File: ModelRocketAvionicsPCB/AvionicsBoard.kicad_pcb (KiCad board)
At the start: 2 copper layers, 62 parts, among them CON1 microSD_Card, P1 FTSH-105-01-F-DV, P2 USB_OTG, P3 JST-2, SW1 SW_RST, U1 TM4C123GH6PM, U2 AT25SF161-16Mb_SPI_FLASH, U3 LIS331, U4 L3GD20HTR, U5 MPL3115A2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

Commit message: Began Preliminary Layout
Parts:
- added JP1: Jumper_NO_Small, Avionics:NO_Jumper, F.Cu at (83.7, 126.4)
- added JP2: Jumper_NC_Small, Avionics:NC_Jumper, F.Cu at (86.3, 124.4)
- added JP3: Jumper_NO_Small, Avionics:NO_Jumper, F.Cu at (78.6, 125.2)
- added JP4: Jumper_NC_Small, Avionics:NC_Jumper, F.Cu at (80.5, 124.6)
- moved SW1 114.6 mm to (72.9, 83.3)
- moved C25 103.1 mm to (72.7, 131.3), turned to 90 degrees
- moved Y2 101.8 mm to (89.3, 85.2)
- moved C13 100.1 mm to (76.7, 92.0), turned to 90 degrees
- moved D1 94.7 mm to (95.2, 53.5)
- moved C11 94.0 mm to (75.1, 92.0), turned to 90 degrees
- moved C32 90.5 mm to (106.6, 56.8), turned to 180 degrees
- moved U4 88.9 mm to (75.5, 125.2), turned to 180 degrees
- moved P2 86.8 mm to (71.3, 94.1), turned to 270 degrees
- moved C16 83.5 mm to (88.8, 77.0)
- moved U7 82.1 mm to (105.8, 54.5), turned to 90 degrees
- moved U1 81.5 mm to (99.8, 99.2), turned to 135 degrees
- moved R7 80.4 mm to (66.9, 85.6), turned to 270 degrees
- moved U3 79.7 mm to (83.3, 123.6)
- moved R3 78.7 mm to (73.0, 113.5), turned to 270 degrees
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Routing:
- added copper zone on B.Cu, net PWR_GND
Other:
- net class Default: clearance 0.2 -> 0.15
- rule trace_clearance: 0.2 -> 0.15
- rule trace_min: 0.2 -> 0.15

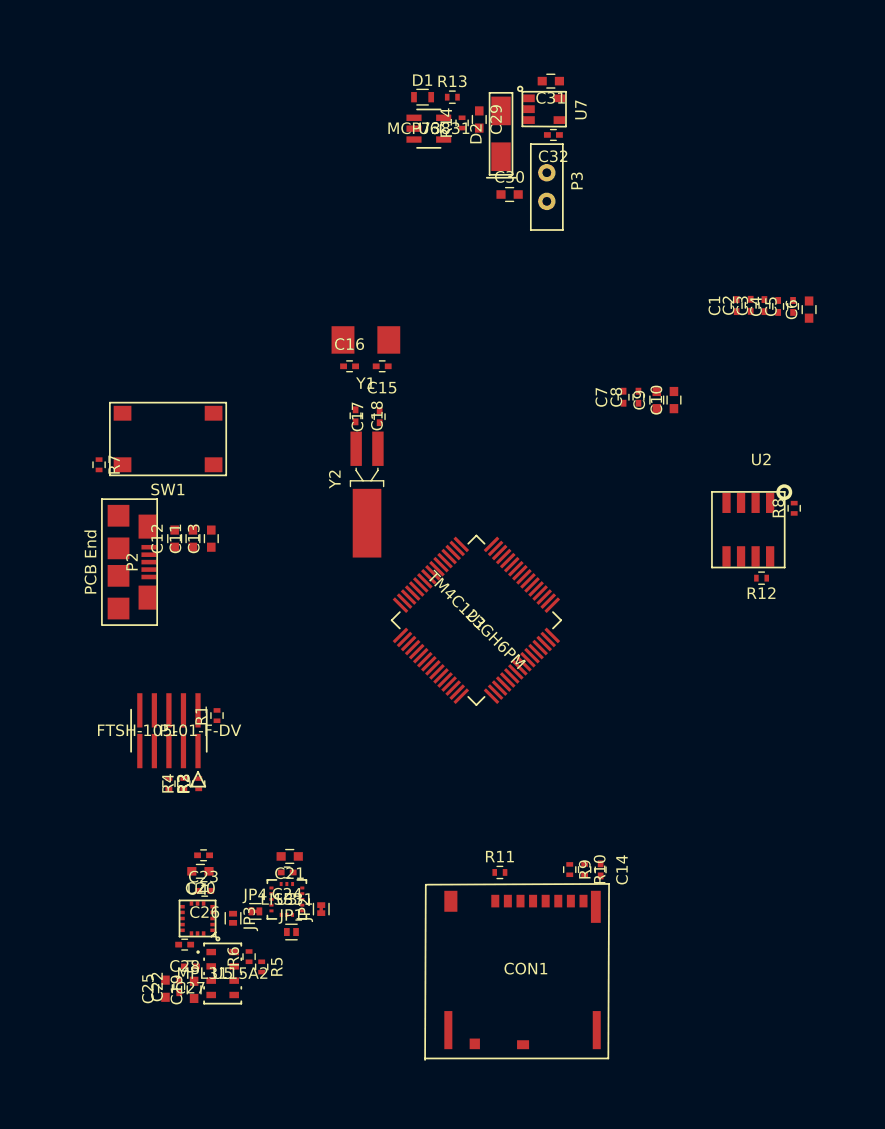
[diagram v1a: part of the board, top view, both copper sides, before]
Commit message: Completed Preliminary Layout
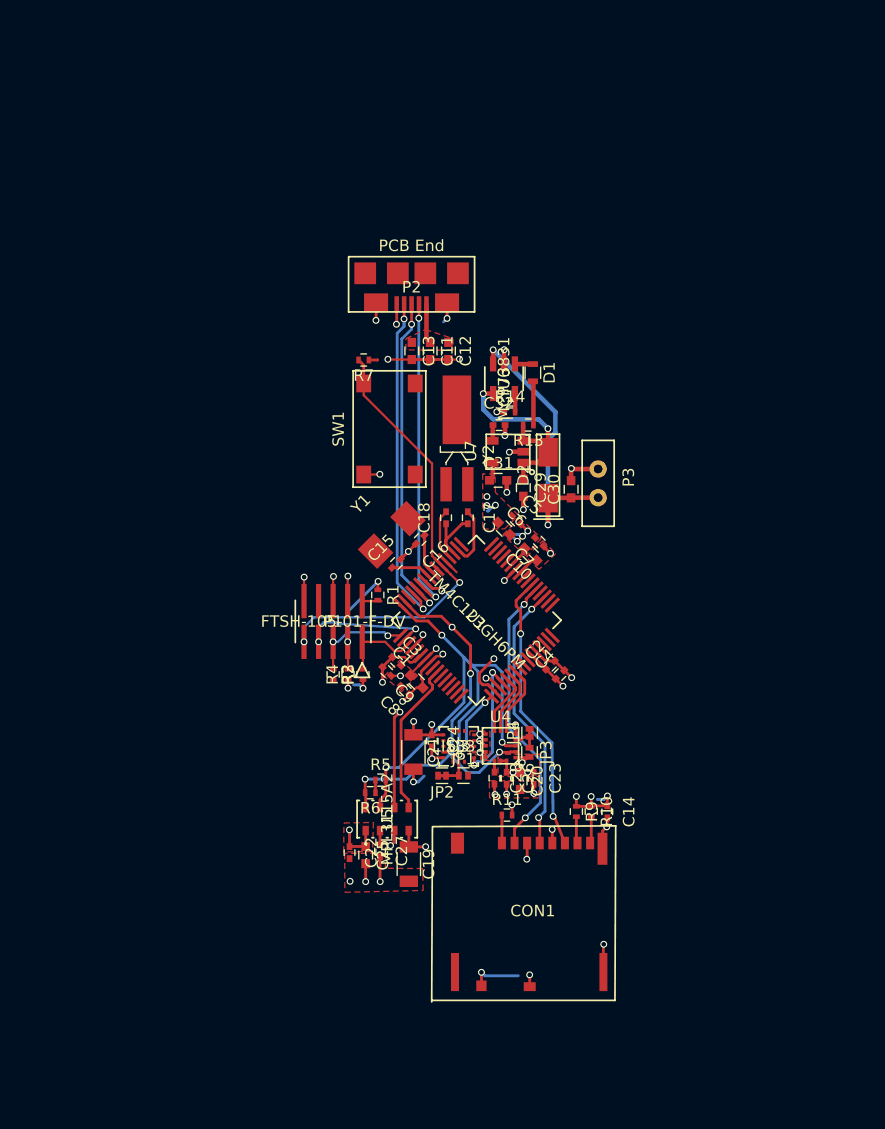
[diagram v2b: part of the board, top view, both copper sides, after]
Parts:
- removed R12, R8: 10k, SFUSAT-Res:R_0402
- removed U2: AT25SF161-16Mb_SPI_FLASH, Avionics:Flash_Mem_AT25SF161-SSHD
- C19, C21: footprint SFUSAT Caps:C_0603 -> SFUSAT Caps:C_1206
- moved C3 44.7 mm to (92.9, 102.8), turned to 315 degrees
- moved C1 44.2 mm to (92.0, 103.7), turned to 315 degrees
- moved C4 37.4 mm to (107.1, 103.9), turned to 45 degrees
- moved C2 36.0 mm to (106.3, 103.1), turned to 45 degrees
- moved C31 35.2 mm to (101.8, 87.0), turned to 0 degrees
- moved C6 32.8 mm to (102.3, 91.2), turned to 315 degrees
- moved C8 32.7 mm to (93.6, 105.3), turned to 135 degrees
- moved C29 32.4 mm to (104.0, 87.6)
- moved C9 32.3 mm to (94.6, 104.5), turned to 135 degrees
- moved P2 32.1 mm to (94.2, 71.6), turned to 180 degrees
- moved C28 30.7 mm to (101.4, 113.0), turned to 270 degrees
- moved C5 30.5 mm to (103.3, 90.4), turned to 315 degrees
- moved U4 30.5 mm to (102.0, 110.1)
- moved D2 30.1 mm to (106.1, 86.5)
- moved U7 30.1 mm to (102.6, 84.5), turned to 270 degrees
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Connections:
- U1 pad 1: Net-(U1-Pad1) -> PB6/ACC_INT1
- U1 pad 4: Net-(U1-Pad4) -> PB7/ACC_INT2
- U1 pad 5: Net-(U1-Pad5) -> PE2/GYR_DEN
- U1 pad 57: Net-(U1-Pad57) -> PB5/BAR_INT1
- U1 pad 58: Net-(U1-Pad58) -> PB4/BAR_INT2
- U1 pad 6: Net-(U1-Pad6) -> PF4/GYR_INT1
- U1 pad 7: Net-(U1-Pad7) -> PE3/GYR_INT2/DRDY
- U3 pad 11: /Sensors/ACC_INT1 -> PB6/ACC_INT1
- U3 pad 9: /Sensors/ACC_INT2 -> PB7/ACC_INT2
- U4 pad 6: /Sensors/GYR_INT2/DRDY -> PE3/GYR_INT2/DRDY
- U4 pad 7: /Sensors/GYR_INT1 -> PF4/GYR_INT1
- U4 pad 8: /Sensors/GYR_DEN -> PE2/GYR_DEN
- U5 pad 5: /Sensors/BAR_INT2 -> PB4/BAR_INT2
- U5 pad 6: /Sensors/BAR_INT1 -> PB5/BAR_INT1
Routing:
- net PWR_GND: track 0.00 -> 74.8 mm, vias 0 -> 41
- net ACC_CS: track 0.00 -> 56.2 mm, vias 0 -> 20
- net PB3/I2C_SDA: track 0.00 -> 45.6 mm, vias 0 -> 4
- net RESET: track 0.00 -> 39.6 mm, vias 0 -> 2
- net PB2/I2C_SCL: track 0.00 -> 36.8 mm, vias 0 -> 5
- net PB0/USB0_ID: track 0.00 -> 29.6 mm, vias 0 -> 2
- net PD5/USB0_DP: track 0.00 -> 29.2 mm, vias 0 -> 2
- net PD4/USB0_DM: track 0.00 -> 28.0 mm, vias 0 -> 2
- net /Power/+VBAT: track 0.00 -> 25.8 mm, vias 0 -> 2
- net PA4/SDDO: track 0.00 -> 25.3 mm, vias 0 -> 2
- net PA5/SDDI: track 0.00 -> 24.7 mm, vias 0 -> 2
- net PA2/SDCLK: track 0.00 -> 24.0 mm, vias 0 -> 2
- net +USB_VBUS: track 0.00 -> 22.4 mm, vias 0 -> 2
- net PB4/BAR_INT2: track 0.00 -> 13.6 mm
- net PC2/JTAG_TDI: track 0.00 -> 11.3 mm, vias 0 -> 2
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- added copper zone on F.Cu, net +USB_VBUS
- added copper zone on F.Cu, net ACC_CS
- added copper zone on PWR.Cu, net ACC_CS
- added copper zone on F.Cu, net PWR_GND
- added copper zone on GND, net PWR_GND
- added copper zone on F.Cu, net PWR_VDDC
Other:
- copper layers 2 -> 4

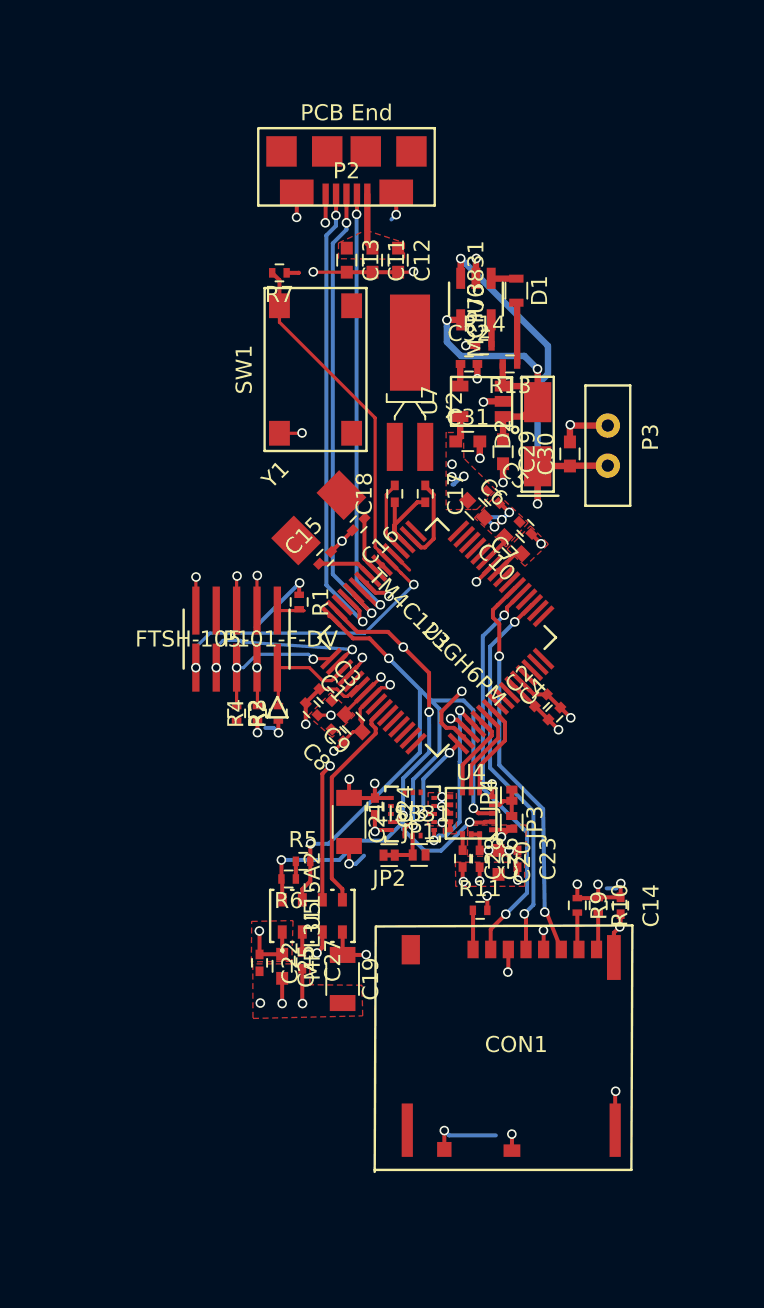
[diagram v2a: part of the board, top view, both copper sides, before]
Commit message: Partially Complete Updated Avionics Layout
Final Pinout and Silk Screen still needs to be completed.
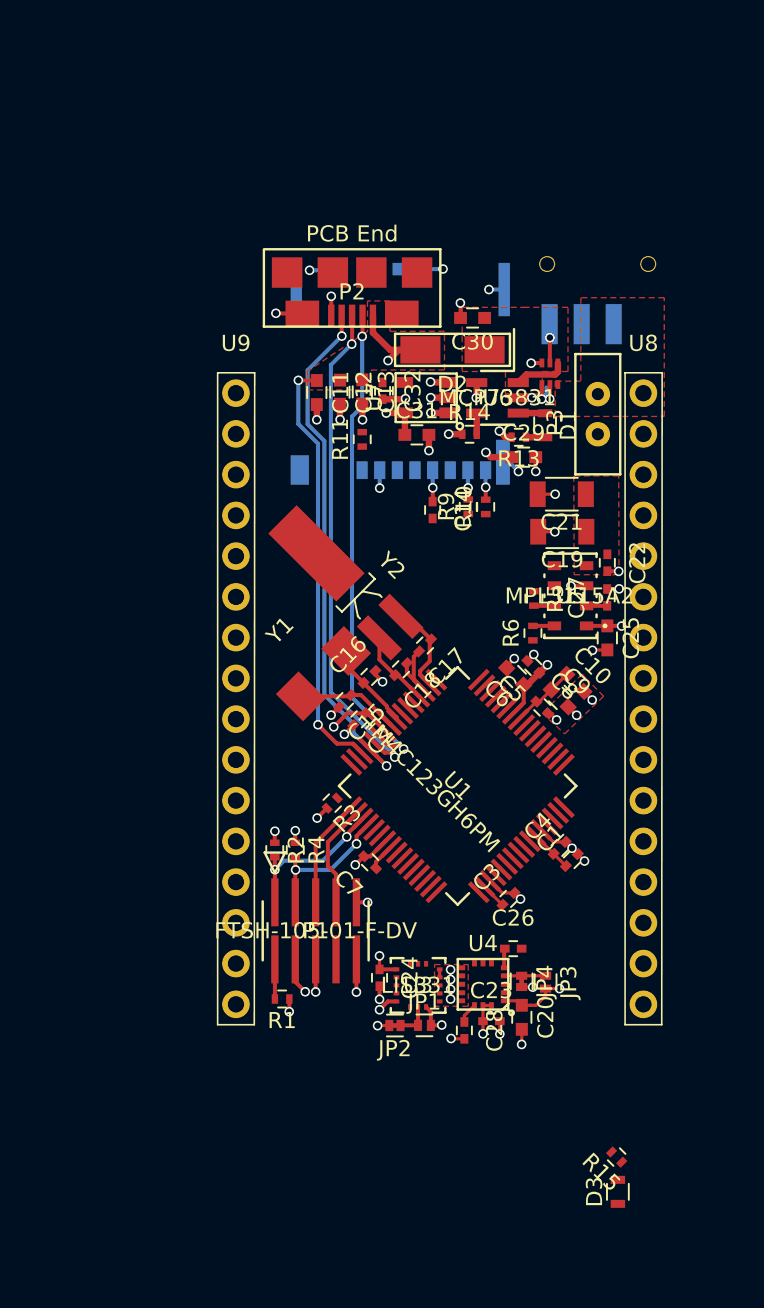
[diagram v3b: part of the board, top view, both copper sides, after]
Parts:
- removed R7: 10k, SFUSAT-Res:R_0402
- removed SW1: SW_RST, Avionics:Push_Button_B3S-1000
- added D3: Led_Small, SFUSAT-Res:R_0603, F.Cu at (111.1, 133.7)
- added R15: 330, SFUSAT-Res:R_0402, F.Cu at (111.0, 131.6)
- added U10: DMG1029SV-7, AvionicsIC:SOT563, F.Cu at (106.9, 82.7)
- added U11: CSS-1210TB, Avionics:CSS-1210TB, B.Cu at (109.8, 77.2)
- added U8: CONNHeaderFemale16, Avionics:16x1_Female_Header, F.Cu at (112.7, 103.0)
- added U9: CONNHeaderFemale16, Avionics:16x1_Female_Header, F.Cu at (87.3, 103.0)
- CON1: moved to B.Cu
- moved CON1 52.9 mm to (91.1, 77.5)
- moved C22 33.0 mm to (110.5, 94.5)
- moved C19 31.1 mm to (107.6, 92.6), turned to 180 degrees
- moved R11 30.3 mm to (95.2, 86.8), turned to 90 degrees
- moved C27 29.6 mm to (110.4, 96.7), turned to 90 degrees
- moved C25 28.8 mm to (110.5, 99.2)
- moved C14 27.3 mm to (99.6, 91.2)
- moved R10 25.8 mm to (102.9, 91.0), turned to 90 degrees
- moved R9 25.8 mm to (101.8, 91.0), turned to 90 degrees
- moved U5 25.6 mm to (108.2, 96.6), turned to 180 degrees
- moved R1 24.8 mm to (90.2, 121.7), turned to 180 degrees
- moved C21 24.4 mm to (107.6, 90.2), turned to 180 degrees
- moved C7 23.0 mm to (95.7, 113.2)
- moved R5 21.8 mm to (105.9, 96.7), turned to 270 degrees
- moved R6 21.6 mm to (105.8, 98.9), turned to 90 degrees
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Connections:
- C30 pad 1: /Power/+VBAT -> +VBAT_ON
- D2 pad 2: /Power/+VBAT -> +VBAT_ON
- P3 pad 1: /Power/+VBAT -> +VBAT
- R3 pad 2: Net-(R3-Pad2) -> PWR_GND
- U1 pad 52: PC1/JTAG_TCK -> PC0/JTAG_TCK
- U1 pad 8: Net-(U1-Pad8) -> PE1/IND_LED
- U6 pad 3: /Power/+VBAT -> +VBAT_ON
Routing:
- net PB3/I2C_SDA: track 45.6 -> 1.28 mm, vias 4 -> 0
- net RESET: track 39.6 -> 0.70 mm, vias 2 -> 1
- net PB2/I2C_SCL: track 36.8 -> 1.34 mm, vias 5 -> 0
- net /Power/+VBAT: track 25.8 -> 0.00 mm, vias 2 -> 0
- net PA5/SDDI: track 24.7 -> 0.00 mm, vias 2 -> 0
- net PA4/SDDO: track 25.3 -> 1.12 mm, vias 2 -> 1
- net PA2/SDCLK: track 24.0 -> 0.00 mm, vias 2 -> 0
- net ACC_CS: track 56.2 -> 33.0 mm, vias 20 -> 12
- net PWR_GND: track 74.8 -> 56.0 mm, vias 41 -> 48
- net +USB_VBUS: track 22.4 -> 39.2 mm, vias 2 -> 8
- net PB4/BAR_INT2: track 13.6 -> 0.00 mm
- net PB7/ACC_INT2: track 11.1 -> 0.00 mm, vias 2 -> 0
- net PB5/BAR_INT1: track 8.55 -> 0.00 mm, vias 1 -> 0
- net PC0/JTAG_TCK: track 2.41 -> 8.83 mm, vias 1 -> 2
- net PE3/GYR_INT2/DRDY: track 6.11 -> 0.00 mm
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- added copper zone on PWR.Cu, net +USB_VBUS
- added copper zone on F.Cu, net +VBAT
- added copper zone on F.Cu, net +VBAT_ON
- removed copper zone on F.Cu, net PWR_VDDC

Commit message: CDR Ready Board
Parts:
- Off U11 On: renamed from U11
- U10: value DMG1029SV-7 -> PMOS
- moved C24 8.21 mm to (99.5, 127.9), turned to 0 degrees
- moved R15 7.87 mm to (109.9, 123.8), turned to 90 degrees
- moved D3 7.52 mm to (109.9, 126.3)
- moved JP3 7.27 mm to (100.0, 117.6), turned to 0 degrees
- moved C26 6.68 mm to (98.0, 119.6), turned to 90 degrees
- moved JP2 6.38 mm to (102.5, 127.0), turned to 270 degrees
- moved JP4 5.60 mm to (99.7, 119.1), turned to 0 degrees
- moved U8 5.00 mm to (112.7, 108.0), turned to 180 degrees
- moved U9 5.00 mm to (87.3, 108.0), turned to 180 degrees
- moved U3 4.84 mm to (100.0, 125.5), turned to 90 degrees
- moved C20 4.59 mm to (102.6, 119.0), turned to 0 degrees
- moved R11 4.33 mm to (95.5, 91.2), turned to 270 degrees
- moved JP1 3.85 mm to (102.5, 125.1), turned to 90 degrees
- moved U4 2.87 mm to (99.9, 121.5), turned to 270 degrees
- moved C23 2.37 mm to (102.2, 121.0), turned to 90 degrees
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- renumbered CON1 to microSD_Card
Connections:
- net Net-(U1-Pad28) renamed PF0
- net Net-(U1-Pad29) renamed PF1
- net PD4/USB0_DM renamed USB0_D-
- net PD5/USB0_DP renamed USB0_D+
- net PE2/GYR_DEN renamed PF4/GYR_DEN
- U1 pad 1: PB6/ACC_INT1 -> PB6/GYR_INT2/DRDY
- U1 pad 10: Net-(U1-Pad10) -> PD7
- U1 pad 13: Net-(U1-Pad13) -> PC7
- U1 pad 14: Net-(U1-Pad14) -> PC6
- U1 pad 15: Net-(U1-Pad15) -> PC5
- U1 pad 16: Net-(U1-Pad16) -> PC4
- U1 pad 17: Net-(U1-Pad17) -> PA0/U0Rx
- U1 pad 18: Net-(U1-Pad18) -> PA1/U0Tx
- U1 pad 23: Net-(U1-Pad23) -> PA6
- U1 pad 24: Net-(U1-Pad24) -> PA7
- U1 pad 30: Net-(U1-Pad30) -> PF2/BAR_INT1
- U1 pad 31: Net-(U1-Pad31) -> PF3/BAR_INT2
- U1 pad 33: Net-(U1-Pad33) -> HIB
- U1 pad 4: PB7/ACC_INT2 -> PB7/GYR_INT1
- U1 pad 53: Net-(U1-Pad53) -> PD6
- U1 pad 57: PB5/BAR_INT1 -> PB5
- U1 pad 58: PB4/BAR_INT2 -> PB4
- U1 pad 59: Net-(U1-Pad59) -> PE4
- U1 pad 6: PF4/GYR_INT1 -> PE3/ACC_INT1
- U1 pad 60: Net-(U1-Pad60) -> PE5
- U1 pad 7: PE3/GYR_INT2/DRDY -> PE2/ACC_INT2
- U1 pad 9: Net-(U1-Pad9) -> PE0
- U3 pad 11: PB6/ACC_INT1 -> PE3/ACC_INT1
- U3 pad 9: PB7/ACC_INT2 -> PE2/ACC_INT2
- U4 pad 6: PE3/GYR_INT2/DRDY -> PB6/GYR_INT2/DRDY
- U4 pad 7: PF4/GYR_INT1 -> PB7/GYR_INT1
- U5 pad 5: PB4/BAR_INT2 -> PF3/BAR_INT2
- U5 pad 6: PB5/BAR_INT1 -> PF2/BAR_INT1
- U8 pad 1: Net-(U8-Pad1) -> +VBAT
- U8 pad 10: Net-(U8-Pad10) -> PC4
- U8 pad 11: Net-(U8-Pad11) -> PC5
- U8 pad 12: Net-(U8-Pad12) -> PC6
- U8 pad 13: Net-(U8-Pad13) -> PC7
- U8 pad 14: Net-(U8-Pad14) -> PD7
- U8 pad 15: Net-(U8-Pad15) -> PE0
- U8 pad 16: +VBAT -> PWR_GND
- U8 pad 2: Net-(U8-Pad2) -> +VBAT
- U8 pad 3: Net-(U8-Pad3) -> ACC_CS
- U8 pad 4: Net-(U8-Pad4) -> ACC_CS
- U8 pad 5: Net-(U8-Pad5) -> WAKE
- U8 pad 6: Net-(U8-Pad6) -> PA7
- U8 pad 7: Net-(U8-Pad7) -> PA6
- U8 pad 8: Net-(U8-Pad8) -> PA1/U0Tx
- U8 pad 9: Net-(U8-Pad9) -> PA0/U0Rx
- U9 pad 1: Net-(U9-Pad1) -> PWR_GND
- U9 pad 10: Net-(U9-Pad10) -> PE4
- U9 pad 11: Net-(U9-Pad11) -> PE5
- U9 pad 12: Net-(U9-Pad12) -> PD0/SSI1CLK
- U9 pad 13: Net-(U9-Pad13) -> PD1/SSI1Fss
- U9 pad 14: Net-(U9-Pad14) -> PD2/SSI1Rx
- U9 pad 15: Net-(U9-Pad15) -> PD3/SSI1Tx
- U9 pad 16: Net-(U9-Pad16) -> ACC_CS
- U9 pad 2: Net-(U9-Pad2) -> PWR_GND
- U9 pad 3: Net-(U9-Pad3) -> PB2/I2C_SCL
- U9 pad 4: Net-(U9-Pad4) -> PB3/I2C_SDA
- U9 pad 5: Net-(U9-Pad5) -> PD6
- U9 pad 6: Net-(U9-Pad6) -> RESET
- U9 pad 7: Net-(U9-Pad7) -> HIB
- U9 pad 8: Net-(U9-Pad8) -> PB5
- U9 pad 9: Net-(U9-Pad9) -> PB4
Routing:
- net PB2/I2C_SCL: track 1.34 -> 71.3 mm, vias 0 -> 3
- net PB3/I2C_SDA: track 1.28 -> 68.6 mm, vias 0 -> 5
- net RESET: track 0.70 -> 31.0 mm, vias 1 -> 4
- net PA2/SDCLK: track 0.00 -> 26.8 mm, vias 0 -> 1
- net PA4/SDDO: track 1.12 -> 26.1 mm
- net HIB: track 0.00 -> 21.8 mm, vias 0 -> 1
- net PA5/SDDI: track 0.00 -> 20.6 mm, vias 0 -> 1
- net PD1/SSI1Fss: track 0.00 -> 20.4 mm
- net PA3/SD~CS: track 1.83 -> 21.6 mm, vias 1 -> 2
- net PF3/BAR_INT2: track 0.00 -> 19.1 mm, vias 0 -> 2
- net PD2/SSI1Rx: track 0.00 -> 18.8 mm
- net PD3/SSI1Tx: track 0.00 -> 18.6 mm
- net PD6: track 0.00 -> 18.3 mm
- net PF2/BAR_INT1: track 0.00 -> 18.1 mm, vias 0 -> 2
- net PB4: track 0.00 -> 17.6 mm, vias 0 -> 1
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- removed copper zone on B.Cu, net PWR_GND
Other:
- board text added: "+ -"
- board text added: "Gyro"

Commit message: Pushed
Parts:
- moved JP3 0.12 mm to (100.0, 117.5)
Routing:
- net PWR_GND: track 71.8 -> 71.3 mm, vias 60 -> 59
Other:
- board outline added: 30 x 55 mm
